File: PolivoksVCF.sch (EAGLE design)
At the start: 42 parts, among them IC1 TL072P, IC2 LM4250P, IC3 LM4250P, Q1 2N3904

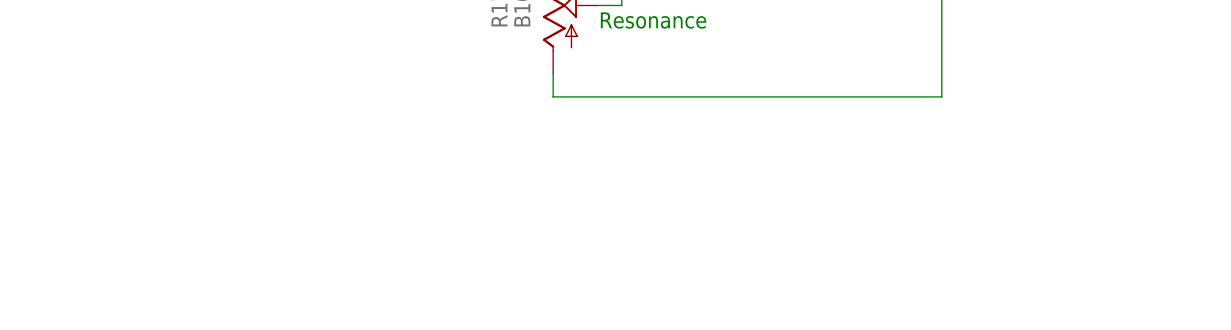
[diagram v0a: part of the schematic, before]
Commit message: added link to original schematic
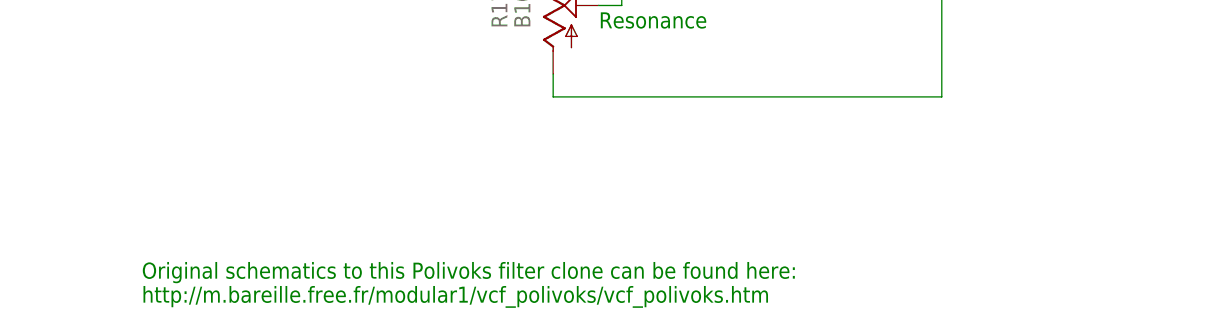
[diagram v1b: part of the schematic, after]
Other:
- note added: "Original schematics to this Polivoks filter clone can be found here: http://m.bareille.free.fr/modular1/vcf_polivoks/vcf_polivoks.htm"
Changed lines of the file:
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@@
 controlled
 resonance</text>
+<text x="7.62" y="2.54" size="1.778" layer="91">Original schematics to this Polivoks filter clone can be found here:
+http://m.bareille.free.fr/modular1/vcf_polivoks/vcf_polivoks.htm
+</text>
 </plain>
 <instances>

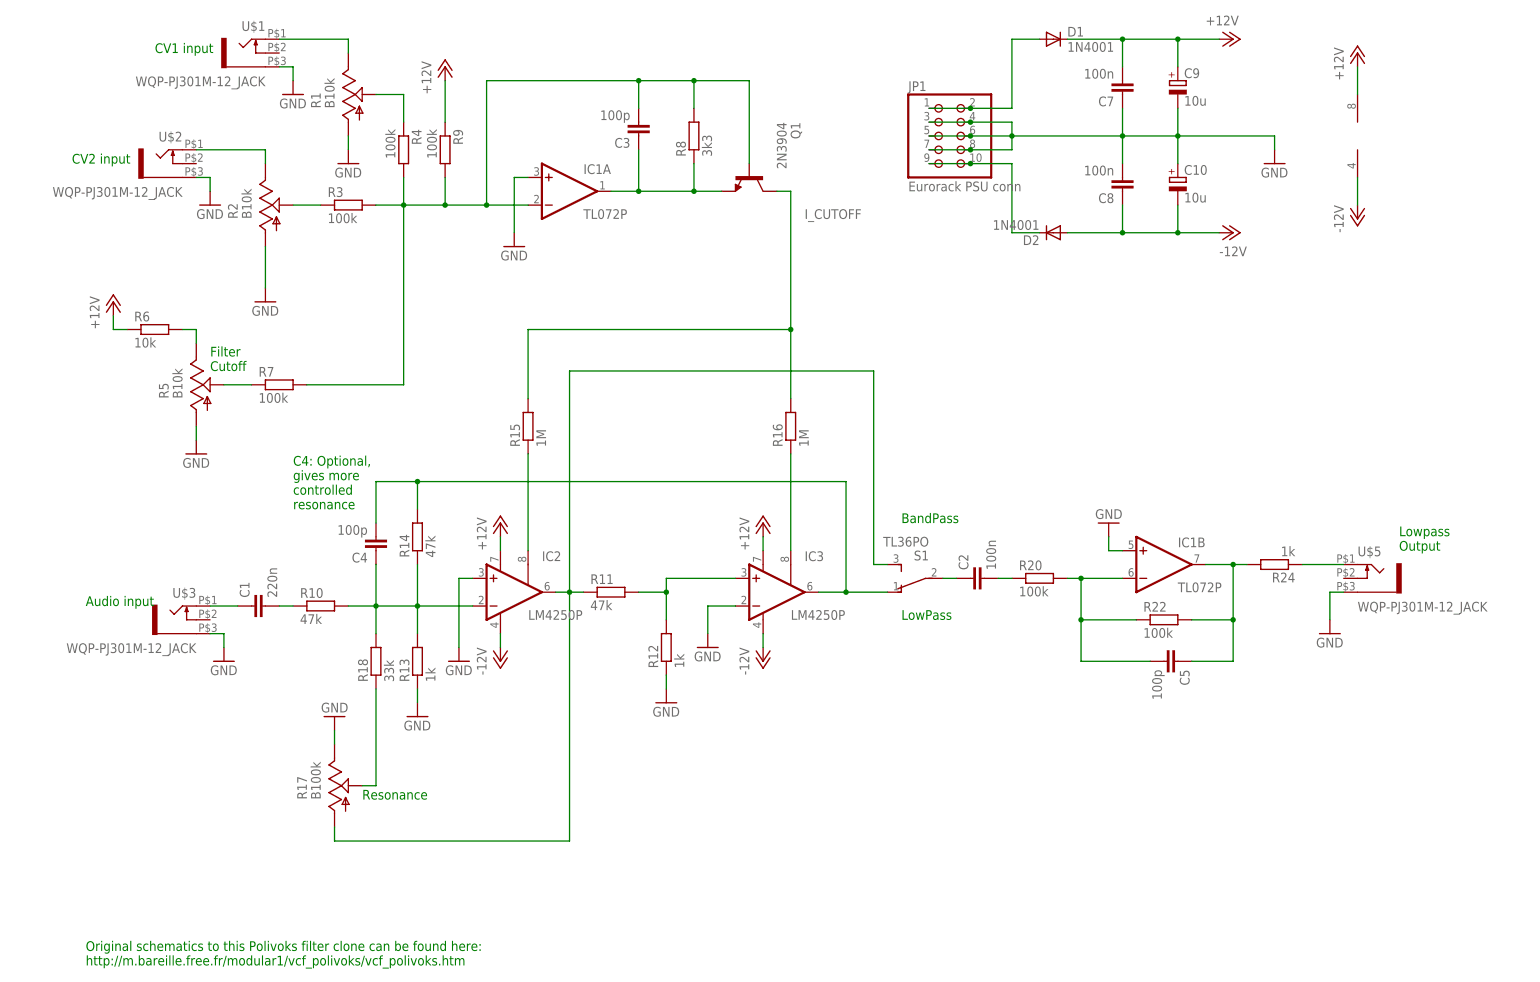
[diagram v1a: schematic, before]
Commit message: Added board file & modified schematic, changed component footprints to vertical on all resistors.
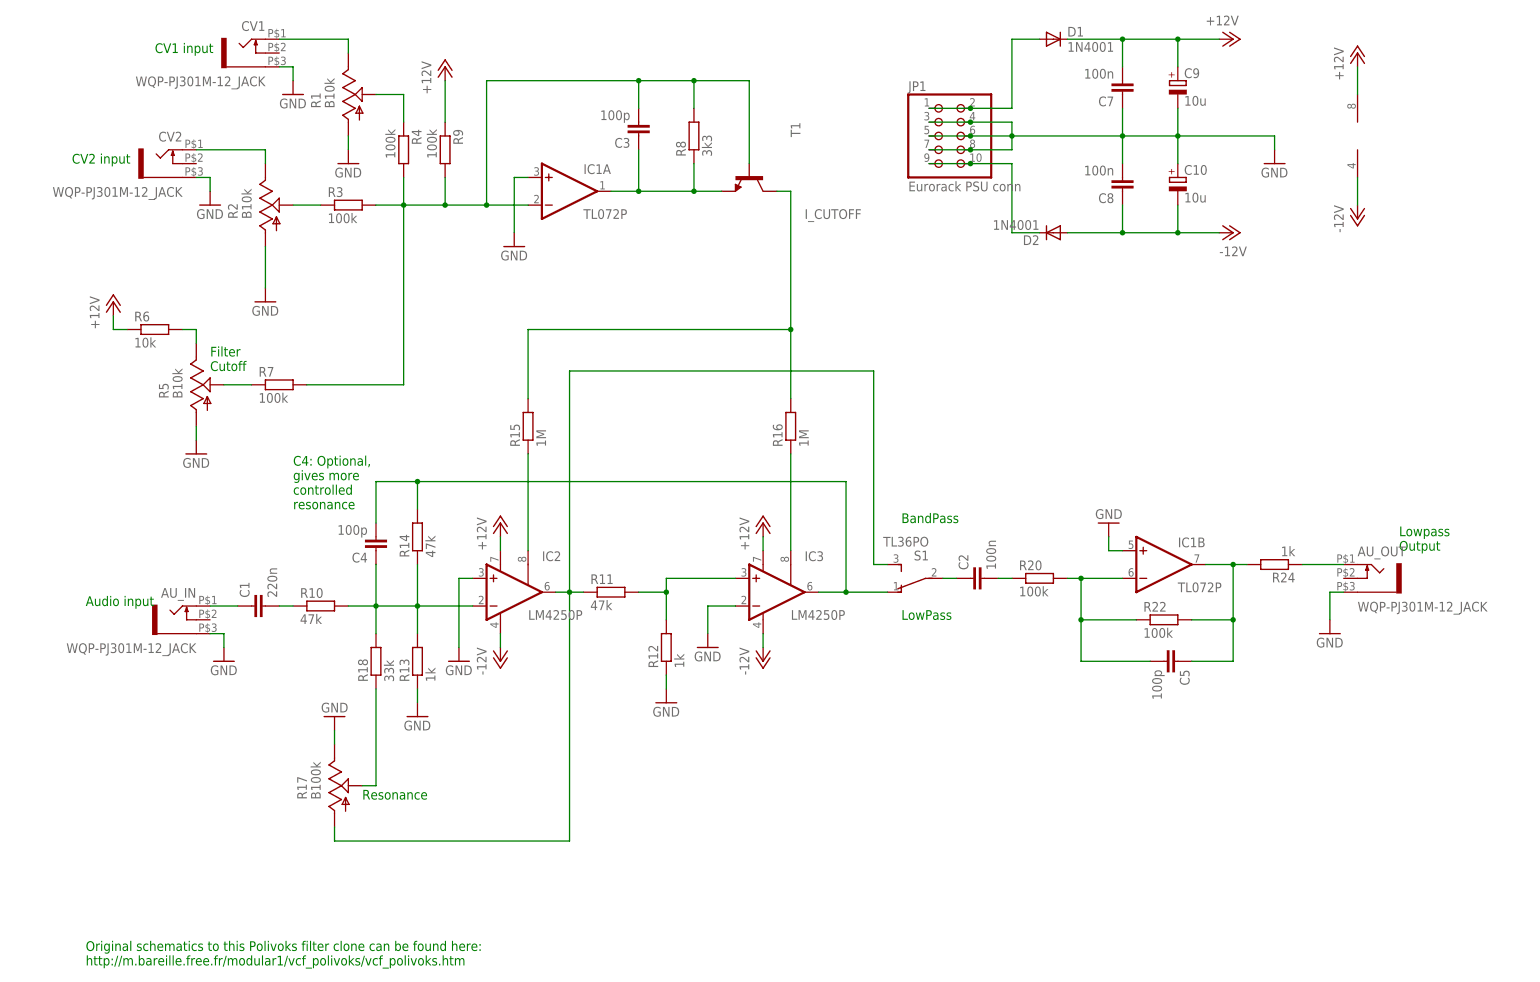
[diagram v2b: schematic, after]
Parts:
- removed Q1: 2N3904, transistor-npn:2N3904
- added T1: (no value), transistor-neu-to92:2N3904-NPN-TO92-EBC
- C2: device rcl:C-EU050-045X075 -> rcl:C-EU050-025X075
- R10, R11, R12, R13, R14, R15, R16, R18, R20, R22, R24, R3, R4, R6, R7, R8, R9: device rcl:R-EU_0207/7 -> rcl:R-EU_0207/2V
- renumbered U$1 to CV1, U$2 to CV2, U$3 to AU_IN, U$5 to AU_OUT
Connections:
- net I_CUTOFF: now also T1.C; no longer Q1.C
- net N$7: now also T1.B; no longer Q1.B
- net N$8: now also T1.E; no longer Q1.E

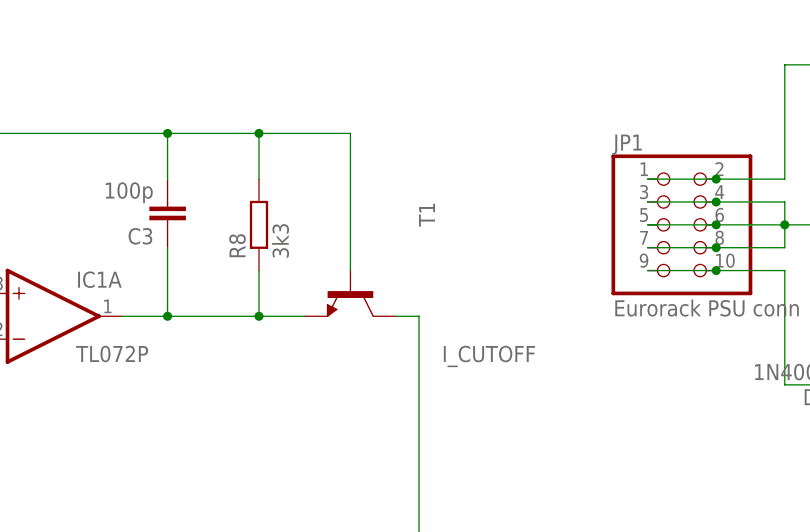
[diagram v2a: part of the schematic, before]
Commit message: Added value to T1 so it shows up on schematic.
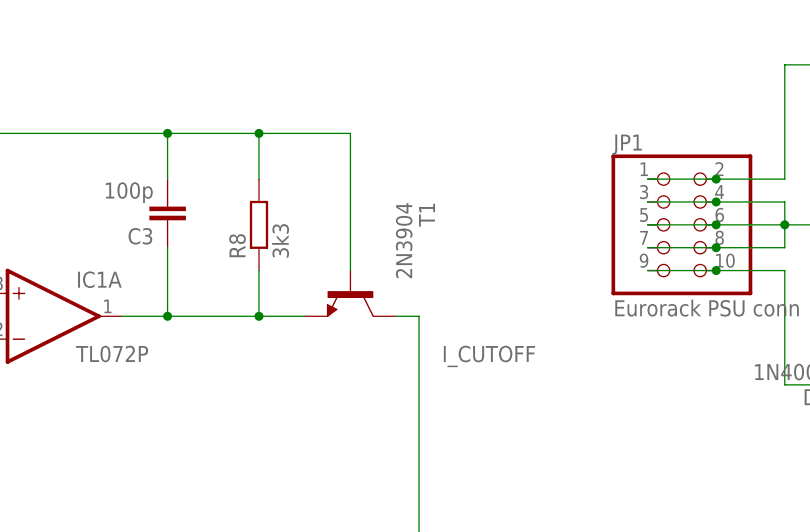
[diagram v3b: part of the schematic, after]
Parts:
- T1: value (none) -> 2N3904
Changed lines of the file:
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@@
 <part name="S1" library="switch" library_urn="urn:adsk.eagle:library:380" deviceset="TL36PO" device="" package3d_urn="urn:adsk.eagle:package:27745/1"/>
 <part name="C4" library="rcl" library_urn="urn:adsk.eagle:library:334" deviceset="C-EU" device="025-025X050" package3d_urn="urn:adsk.eagle:package:23629/2" value="100p"/>
-<part name="T1" library="transistor-neu-to92" deviceset="*-NPN-" device="TO92-EBC" technology="2N3904"/>
+<part name="T1" library="transistor-neu-to92" deviceset="*-NPN-" device="TO92-EBC" technology="2N3904" value="2N3904"/>
 </parts>
 <sheets>

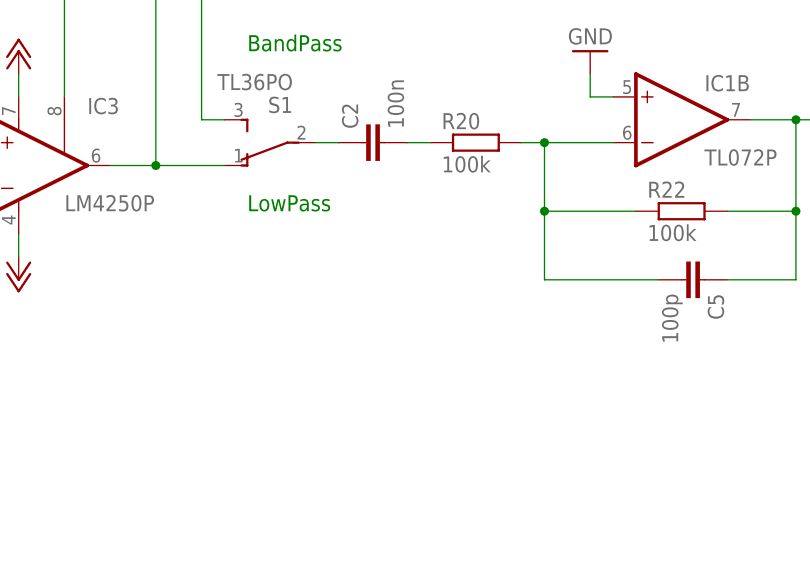
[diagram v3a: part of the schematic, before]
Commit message: Added note about type of S1.
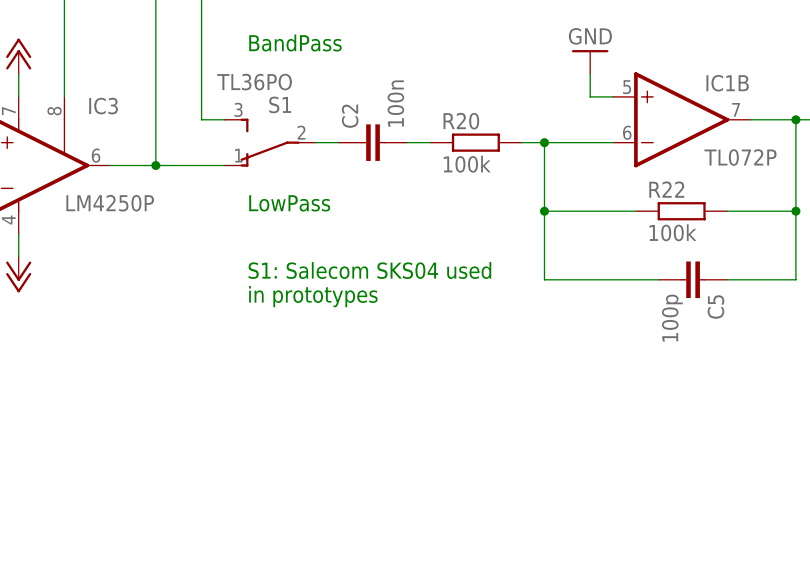
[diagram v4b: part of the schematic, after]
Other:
- note added: "S1: Salecom SKS04 used in prototypes"
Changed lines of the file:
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@@
 http://m.bareille.free.fr/modular1/vcf_polivoks/vcf_polivoks.htm
 </text>
+<text x="157.48" y="55.88" size="1.778" layer="91">S1: Salecom SKS04 used
+in prototypes</text>
 </plain>
 <instances>
